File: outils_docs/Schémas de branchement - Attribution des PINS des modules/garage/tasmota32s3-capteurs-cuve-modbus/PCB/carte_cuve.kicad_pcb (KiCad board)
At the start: 2 copper layers, 100 x 100 mm, 49 parts, among them J1 Entree 12 V, J10 Voie A0 (+12V / entree / GND), J11 Voie A1 (+12V / entree / GND), J12 Voie A2 (+12V / entree / GND), J13 Voie A3 (+12V / entree / GND), J14 Extension GPIO (3V3 GND 7 15 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, J4 Module ADS1115, J5 Module RS485 auto (VCC TX RX 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, J7 DS18B20 (3V3 / DQ / GND), J8 Ruban WS2815 (DI / BI / GND), J9 Extension I2C (3V3 GND SCL SD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, U1 TSR 1-2450, U3 74AHCT125

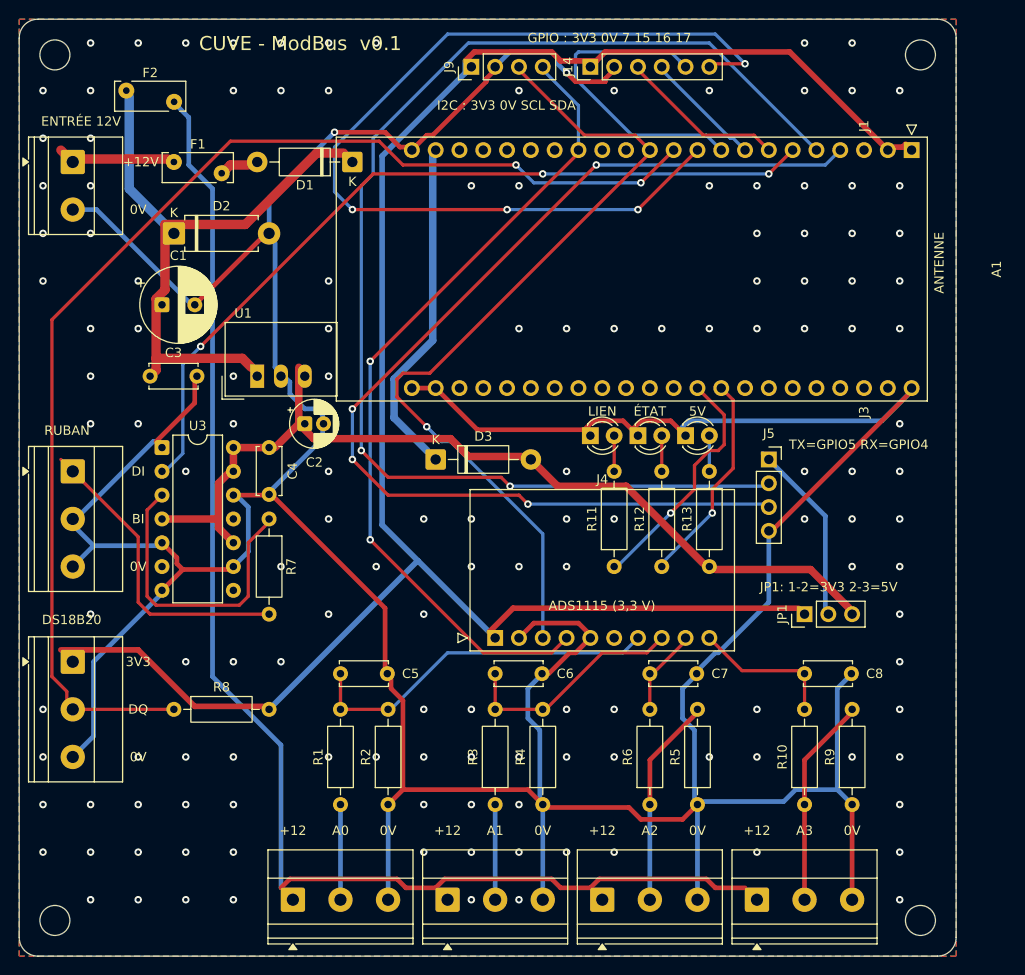
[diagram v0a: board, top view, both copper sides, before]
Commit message: feat: carte cuve v0.2, filtre du bouton du ruban et placement corrige
Bouton du ruban sur GPIO7 (J14 broche 3, cable > 1 m) : R14 rappel
10 k vers 3V3, R15 1 k serie, C9 100 nF vers 0V.

Placement : les 9 erreurs DRC de la v0.1 (D1 et U1 sous le DevKit,
R11-R13 sous l'ADS1115) sont corrigees. D1 au-dessus du DevKit ;
U1, C1, C2 regroupes entre R7 et l'ADS1115, C3 colle sous U1 (boucle
d'entree 3,65 mm) ; F1 hors du trajet des cables USB-C ; R11-R13
debout, LED au pas de 6,35 ; R11 180 ohm (bleue), R12 560 ohm (verte).

Masses des LED et de C9/J14 routees avant les signaux : C9 et J14.2
formaient un ilot sans lien avec la masse.

DRC avec parite : 0 violation, 0 non connecte, 0 ecart ; ERC 0 erreur.
Avant commande : identifier le module RS485, mesurer le DevKit et les
modules, verifier la hauteur des fusibles rearmables.
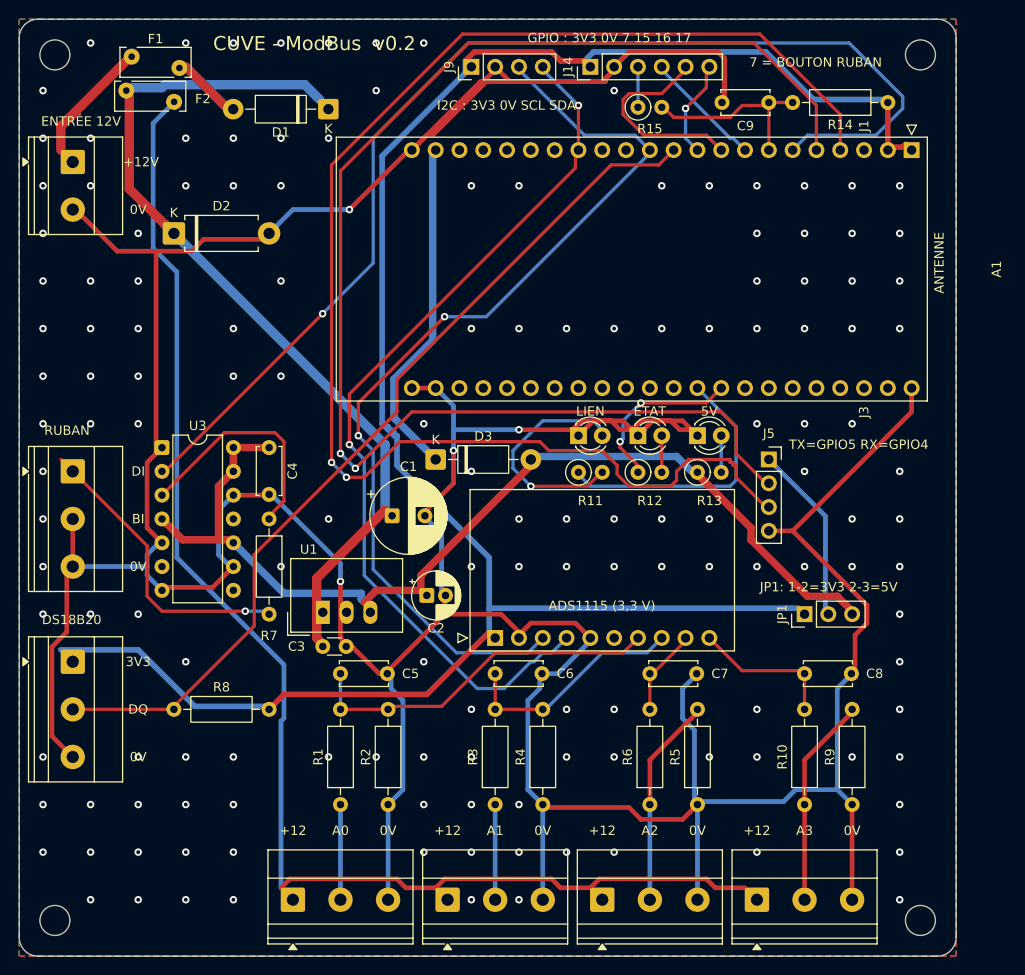
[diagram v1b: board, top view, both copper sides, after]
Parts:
- added C9: 100nF, Capacitor_THT:C_Disc_D5.0mm_W2.5mm_P5.00mm, F.Cu at (180.0, 58.9)
- added R14: 10k, Resistor_THT:R_Axial_DIN0207_L6.3mm_D2.5mm_P10.16mm_Horizontal, F.Cu at (192.7, 58.9)
- added R15: 1k, Resistor_THT:R_Axial_DIN0207_L6.3mm_D2.5mm_P2.54mm_Vertical, F.Cu at (166.0, 59.4)
- C3: value 100nF -> 100nF 50V; footprint Capacitor_THT:C_Disc_D5.0mm_W2.5mm_P5.00mm -> Capacitor_THT:C_Disc_D3.0mm_W1.6mm_P2.50mm
- R11: value 1k -> 180; footprint Resistor_THT:R_Axial_DIN0207_L6.3mm_D2.5mm_P10.16mm_Horizontal -> Resistor_THT:R_Axial_DIN0207_L6.3mm_D2.5mm_P2.54mm_Vertical
- R12: value 1k -> 560; footprint Resistor_THT:R_Axial_DIN0207_L6.3mm_D2.5mm_P10.16mm_Horizontal -> Resistor_THT:R_Axial_DIN0207_L6.3mm_D2.5mm_P2.54mm_Vertical
- R13: footprint Resistor_THT:R_Axial_DIN0207_L6.3mm_D2.5mm_P10.16mm_Horizontal -> Resistor_THT:R_Axial_DIN0207_L6.3mm_D2.5mm_P2.54mm_Vertical
- moved C3 34.2 mm to (132.4, 117.0)
- moved C1 33.3 mm to (139.8, 103.0)
- moved U1 26.2 mm to (132.4, 113.3)
- moved C2 22.5 mm to (143.5, 111.5)
- moved F1 12.1 mm to (112.0, 54.0)
- moved R11 10.8 mm to (159.7, 98.4), turned to 0 degrees
- moved R12 10.4 mm to (166.0, 98.4), turned to 0 degrees
- moved R13 10.1 mm to (172.4, 98.4), turned to 0 degrees
- moved D1 6.19 mm to (133.0, 59.6)
- moved LED1 1.27 mm to (159.7, 94.5)
- moved LED3 1.27 mm to (172.4, 94.5)
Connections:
- J14 pad 3: /GPIO7 -> /BTN_RUBAN
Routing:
- net /GPIO17: track 99.8 -> 9.25 mm, vias 4 -> 1
- net GND: track 442.3 -> 487.5 mm, vias 146 -> 153
- net /RS485_RX: track 114.2 -> 154.2 mm, vias 4 -> 2
- net /WS_DATA_3V3: track 85.9 -> 121.8 mm, vias 3 -> 1
- net /DS18_DQ: track 127.6 -> 92.8 mm, vias 2 -> 0
- net +12V: track 64.4 -> 93.4 mm
- net /LED1_A: track 2.54 -> 23.5 mm, vias 0 -> 1
- net /RS485_TX: track 134.1 -> 146.4 mm
- net /GPIO16: track 32.8 -> 20.7 mm
- net /I2C_SCL: track 87.1 -> 98.8 mm, vias 1 -> 2
- net +5V: track 90.1 -> 98.9 mm
- net /I2C_SDA: track 85.3 -> 92.9 mm
- net /WS_DATA_5V: track 31.0 -> 23.9 mm
- net +3V3: track 201.1 -> 206.8 mm
- net /LED_ETAT: track 21.5 -> 17.2 mm, vias 1 -> 2
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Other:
- board text added: "7 = BOUTON RUBAN"
- board text added: "CUVE - ModBus v0.2"
- board text removed: "CUVE - ModBus v0.1"

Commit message: feat(pcb): carte cuve v0.3, module RS485 XY-017 reel et corrections de la relecture
- Module RS485 XY-017 (confirme) avec son empreinte Modules_Tasmota, debout
  sous le DevKit ; bornier A/B au-dessus du coin bas droit, libere en
  decalant les 4 voies analogiques de 10,16 mm a gauche.
- JP1 supprime : RS485 en 3,3 V fixe (en 5 V, son RXD mettait 5 V sur GPIO4).
- Bornier a vis J15 pour le bouton du ruban (cable > 1 m).
- Voies dans l'ordre entree / 0V / +12 : un brin entre bornes voisines ne
  brule plus le shunt ; type de voie (0-10V, 4-20mA) serigraphie.
- R16 10 k de rappel sur l'entree du 74AHCT125, C1 en 35 V, R8 debout.
- DRC parite 0, 0 non connecte, 0 violation ; ERC 0 erreur ; masse en 1 groupe.
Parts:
- removed JP1: VCC RS485 : 1-2 = 3V3 (defaut), 2-3 = 5V, Connector_PinHeader_2.54mm:PinHeader_1x03_P2.54mm_Vertical
- added J15: Bouton du ruban (BTN / GND), TerminalBlock_Phoenix:TerminalBlock_Phoenix_MKDS-1,5-2-5.08_1x02_P5.08mm_Horizontal, F.Cu at (105.7, 80.5)
- added R16: 10k, Resistor_THT:R_Axial_DIN0207_L6.3mm_D2.5mm_P2.54mm_Vertical, F.Cu at (115.2, 91.2)
- C1: value 100uF 25V -> 100uF 35V
- J10: value Voie A0 (+12V / entree / GND) -> Voie A0 (entree / GND / +12V)
- J11: value Voie A1 (+12V / entree / GND) -> Voie A1 (entree / GND / +12V)
- J12: value Voie A2 (+12V / entree / GND) -> Voie A2 (entree / GND / +12V)
- J13: value Voie A3 (+12V / entree / GND) -> Voie A3 (entree / GND / +12V)
- J5: value Module RS485 auto (VCC TX RX GND) -> Module RS485 XY-017 (VCC TXD RXD GND); footprint Connector_PinSocket_2.54mm:PinSocket_1x04_P2.54mm_Vertical -> Modules_Tasmota:Module_RS485_Auto_XY-017
- R8: footprint Resistor_THT:R_Axial_DIN0207_L6.3mm_D2.5mm_P10.16mm_Horizontal -> Resistor_THT:R_Axial_DIN0207_L6.3mm_D2.5mm_P2.54mm_Vertical
- moved J5 14.5 mm to (194.5, 95.9), turned to -90 degrees
- moved J13 10.2 mm to (168.6, 144.0)
- moved C6 10.2 mm to (140.6, 119.8)
- moved R3 10.2 mm to (140.6, 133.8)
- moved J10 10.2 mm to (119.0, 144.0)
- moved C5 10.2 mm to (124.1, 119.8)
- moved C7 10.2 mm to (157.2, 119.8)
- moved C8 10.2 mm to (173.7, 119.8)
- moved J11 10.2 mm to (135.6, 144.0)
- moved J12 10.2 mm to (152.1, 144.0)
- moved R1 10.2 mm to (124.1, 133.8)
- moved R10 10.2 mm to (173.7, 133.8)
- moved R2 10.2 mm to (129.2, 133.8)
- moved R4 10.2 mm to (145.7, 133.8)
- moved R5 10.2 mm to (162.2, 133.8)
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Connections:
- J10 pad 1: +12V_CAPT -> /IN0
- J10 pad 2: /IN0 -> GND
- J10 pad 3: GND -> +12V_CAPT
- J11 pad 1: +12V_CAPT -> /IN1
- J11 pad 2: /IN1 -> GND
- J11 pad 3: GND -> +12V_CAPT
- J12 pad 1: +12V_CAPT -> /IN2
- J12 pad 2: /IN2 -> GND
- J12 pad 3: GND -> +12V_CAPT
- J13 pad 1: +12V_CAPT -> /IN3
- J13 pad 2: /IN3 -> GND
- J13 pad 3: GND -> +12V_CAPT
- J5 pad 1: VCC_485 -> +3V3
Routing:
- net /BTN_RUBAN: track 3.17 -> 72.6 mm
- net GND: track 487.5 -> 530.4 mm, vias 153 -> 146
- net +5V: track 98.9 -> 76.5 mm
- net VCC_485: track 19.3 -> 0.00 mm
- net /RS485_RX: track 154.2 -> 172.5 mm, vias 2 -> 3
- net +3V3: track 206.8 -> 223.4 mm
- net /WS_DATA_3V3: track 121.8 -> 108.8 mm, vias 1 -> 3
- net /GPIO16: track 20.7 -> 9.20 mm, vias 0 -> 1
- net /AIN2: track 6.58 -> 16.9 mm
- net /AIN1: track 21.0 -> 31.2 mm
- net /AIN0: track 35.0 -> 45.1 mm
- net +12V_CAPT: track 142.1 -> 151.7 mm
- net /RS485_TX: track 146.4 -> 155.3 mm, vias 2 -> 4
- net /AIN3: track 13.1 -> 5.08 mm
- net /WS_DATA_5V: track 23.9 -> 20.3 mm
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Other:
- board text added: "0-10V"
- board text added: "4-20mA"
- board text added: "BOUTON"
- board text added: "BTN"
- board text added: "CUVE - ModBus v0.3"
- board text added: "RS485 TX=GPIO5 RX=GPIO4"
- board text removed: "CUVE - ModBus v0.2"
- board text removed: "JP1: 1-2=3V3 2-3=5V"
- board text removed: "TX=GPIO5 RX=GPIO4"
- board text removed: "module RS485 (modèle à identifier)"
